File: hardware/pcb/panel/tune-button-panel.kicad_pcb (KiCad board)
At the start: 2 copper layers, 148 x 86.7 mm, 237 parts, among them J1 USB-C, J1 XIAO left, J2 LiPo, J2 XIAO right, J3 Buttons, J3 LiPo, J4 to XIAO BAT, Q1 AO3401A, SW1 MX switch, SW2 MX switch, SW3 MX switch, SW4 MX switch, SW5 RESET, SW6 BOOT, U1 ESP32-C3-WROOM-02-N4, U2 SRV05-4, U3 TP4054, U4 RT9080-3.3, U5 SRV05-4

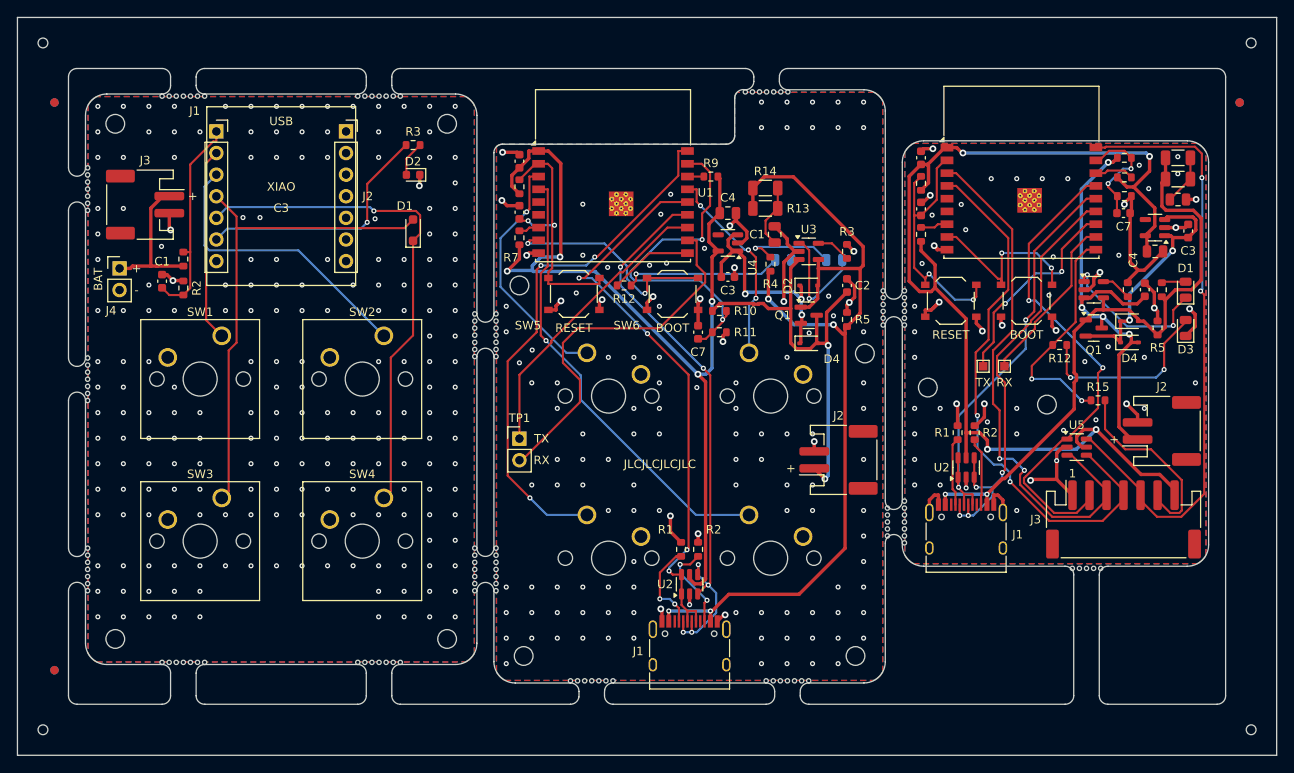
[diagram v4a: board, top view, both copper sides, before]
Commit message: pcb: c3-jst round-8 audit fixes; panel rebuilt with the moved C1
- README: H2 now needs a nylon screw or washers (K2 and VBUS run 1.6 mm from its centre), and the
  c3-jst tab-placement remark follows the new copper.
- Back pour kept off the top edge above the 3V3 track at the antenna base (was a 0.29 mm strip).
- K4 via moved 0.1 mm off K3's (0.60 mm hole to hole).
- panel.py: no tab within 3 mm of an 0805-or-larger ceramic capacitor. Panel rebuilt: c3-jst has six
  tabs, three of them cut-not-snap.
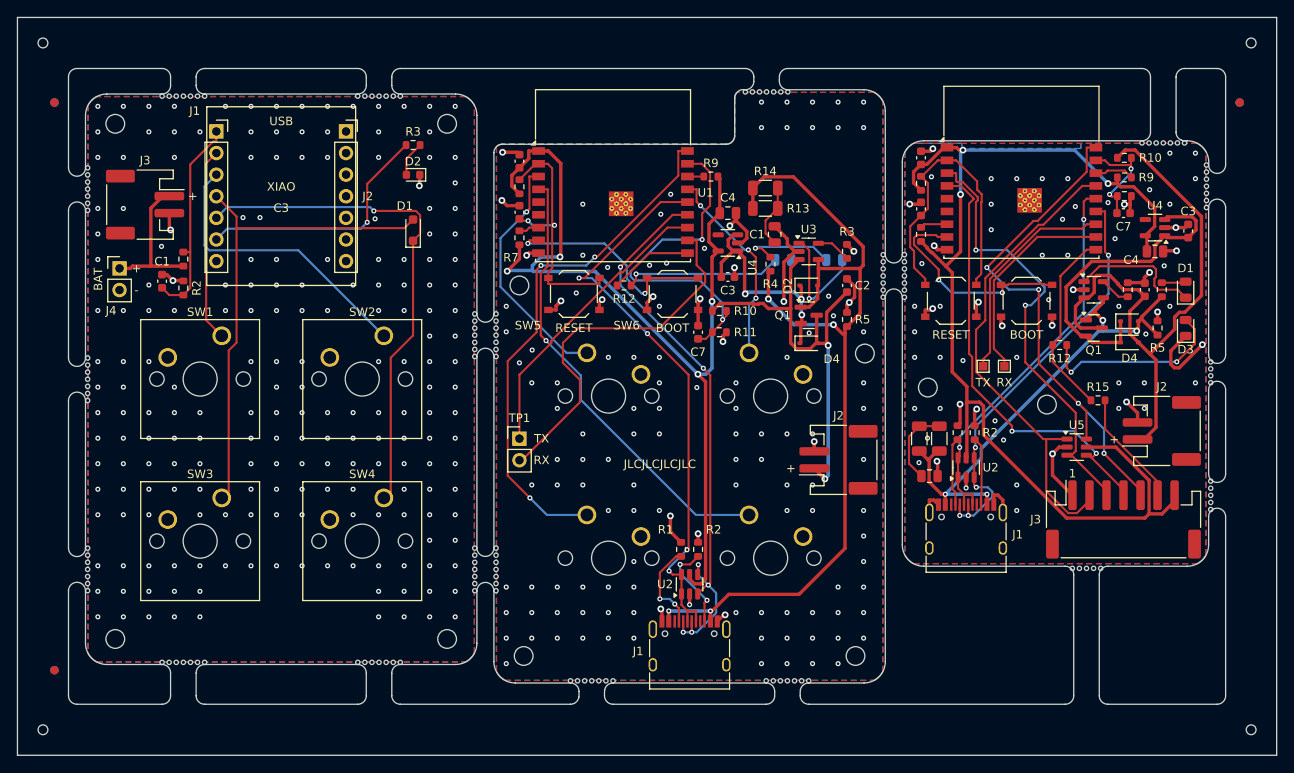
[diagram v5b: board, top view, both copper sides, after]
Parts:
- removed KiKit_MB_19_6: NPTH, NPTH
- added KiKit_MB_12_7: NPTH, NPTH, F.Cu at (101.8, 25.4)
- added KiKit_MB_16_7: NPTH, NPTH, F.Cu at (104.2, 20.4)
- added KiKit_MB_18_1: NPTH, NPTH, F.Cu at (132.2, 7.25)
- added KiKit_MB_18_7: NPTH, NPTH, F.Cu at (137.2, 7.25)
- added KiKit_MB_20_2: NPTH, NPTH, F.Cu at (140.2, 47.0)
- added KiKit_MB_20_3: NPTH, NPTH, F.Cu at (140.2, 47.8)
- added KiKit_MB_20_4: NPTH, NPTH, F.Cu at (140.2, 48.7)
- added KiKit_MB_20_5: NPTH, NPTH, F.Cu at (140.2, 49.5)
- added KiKit_MB_20_6: NPTH, NPTH, F.Cu at (140.2, 50.3)
- added KiKit_MB_21_2: NPTH, NPTH, F.Cu at (127.3, 57.2)
- added KiKit_MB_21_3: NPTH, NPTH, F.Cu at (126.5, 57.2)
- added KiKit_MB_21_4: NPTH, NPTH, F.Cu at (125.7, 57.2)
- added KiKit_MB_21_5: NPTH, NPTH, F.Cu at (124.8, 57.2)
- added KiKit_MB_21_6: NPTH, NPTH, F.Cu at (124.0, 57.2)
- moved KiKit_MB_18_6 57.4 mm to (136.3, 7.25)
- moved KiKit_MB_17_1 56.9 mm to (139.8, 9.84)
- moved KiKit_MB_18_5 56.2 mm to (135.5, 7.25)
- moved KiKit_MB_17_2 55.6 mm to (139.8, 10.7)
- moved KiKit_MB_18_4 55.1 mm to (134.7, 7.25)
- moved KiKit_MB_17_3 54.3 mm to (139.8, 11.5)
- moved KiKit_MB_18_3 53.9 mm to (133.8, 7.25)
- moved KiKit_MB_17_4 53.1 mm to (139.8, 12.3)
- moved KiKit_MB_18_2 52.8 mm to (133.0, 7.25)
- moved KiKit_MB_17_5 51.9 mm to (139.8, 13.2)
- moved KiKit_MB_17_6 50.7 mm to (139.8, 14.0)
- moved KiKit_MB_17_7 49.5 mm to (139.8, 14.8)
- moved R13 44.9 mm to (106.0, 42.0), turned to 90 degrees
- moved C1 43.7 mm to (107.2, 46.4)
- moved R14 41.4 mm to (108.3, 42.0), turned to 90 degrees
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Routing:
- net Board_2-VBAT: track 52.8 -> 69.7 mm, vias 4 -> 0
- net Board_2-GND: track 74.8 -> 58.3 mm, vias 54 -> 64
- net Board_2-K3: track 65.7 -> 51.8 mm
- net Board_2-VBUS: track 73.3 -> 60.9 mm, vias 2 -> 4
- net Board_2-K2: track 64.0 -> 52.2 mm
- net Board_2-K4: track 72.6 -> 61.3 mm, vias 2 -> 4
- net Board_2-VSYS: track 29.0 -> 38.1 mm, vias 2 -> 0
- net Board_2-LED_OUT: track 22.6 -> 13.7 mm
- net Board_2-LED: track 27.0 -> 22.3 mm, vias 2 -> 0
- net Board_2-RXD: track 20.3 -> 24.7 mm
- net Board_2-IO9: track 21.1 -> 25.4 mm
- net Board_2-EN: track 31.4 -> 35.7 mm, vias 2 -> 0
- net Board_2-USB_DP: track 49.3 -> 45.8 mm
- net Board_2-VBUS_C: track 5.89 -> 9.32 mm
- net Board_2-STAT: track 18.3 -> 15.6 mm, vias 2 -> 0
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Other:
- outline, holes or cut-outs redrawn

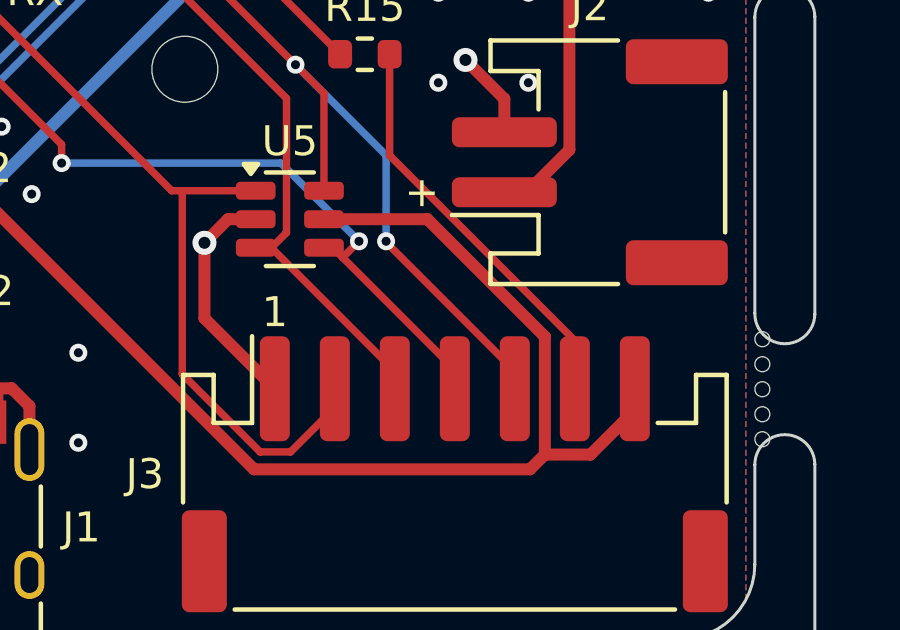
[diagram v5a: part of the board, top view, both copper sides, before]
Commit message: pcb: c3-jst round-9 audit fixes
- README: the single-board right-edge tab windows at 25-29 and 39-45 mm are inside the 2 mm
  connector keep-out, so cut those tabs rather than snapping them; H1's wording names the pour.
- K4: the 0.03 mm stub left by the via move is gone; the diagonal starts at the via, at 45 deg.
- Panel rebuilt with it.
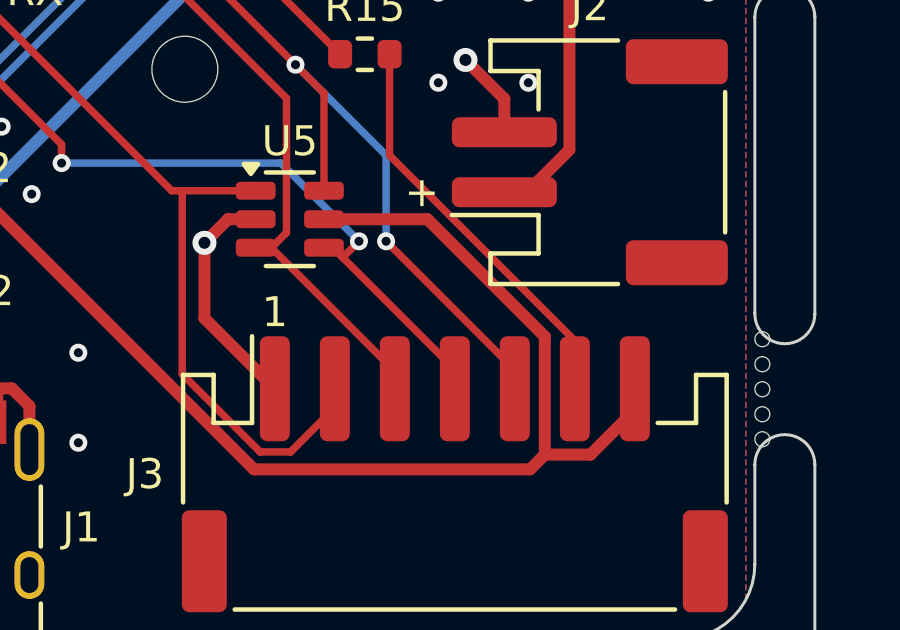
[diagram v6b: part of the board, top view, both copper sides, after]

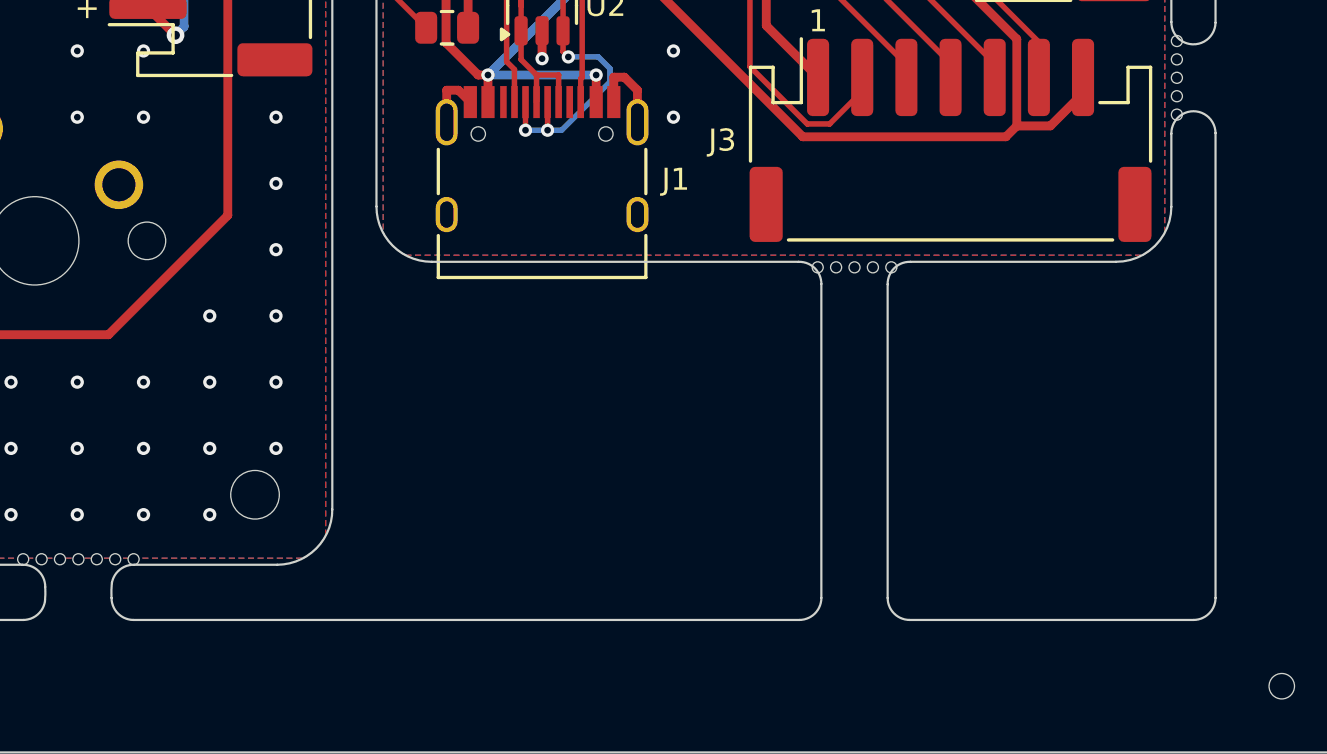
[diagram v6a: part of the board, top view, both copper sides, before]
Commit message: pcb: panel round-7 audit fixes
- Tabs prefer a place at least 2.25 mm from a connector's pads within their free span: c3-jst's
  bottom tab moves clear of J3, leaving two cut-don't-snap tabs (both on c3-jst's right edge).
- Note that pour a tab keepout cuts off is dropped as an island.
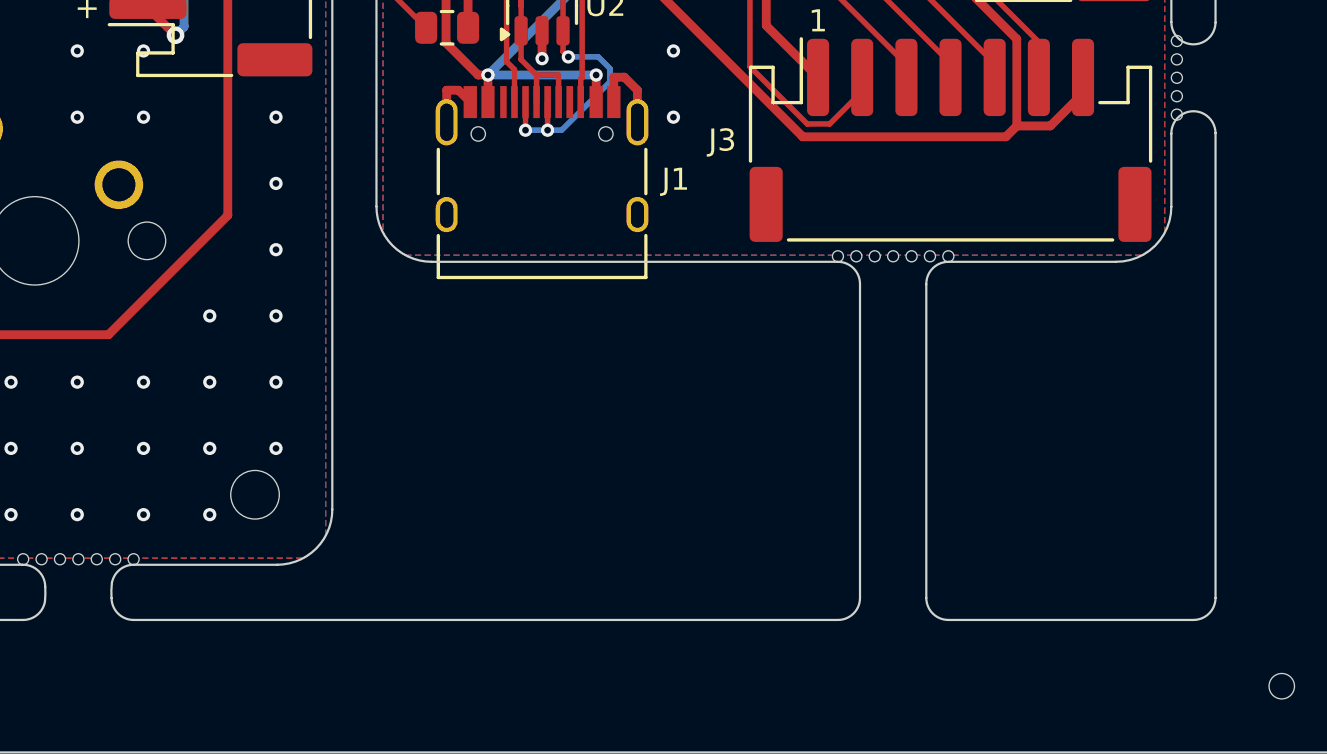
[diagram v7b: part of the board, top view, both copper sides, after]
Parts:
- removed KiKit_MB_20_6: NPTH, NPTH
- added KiKit_MB_19_1: NPTH, NPTH, F.Cu at (129.9, 56.8)
- added KiKit_MB_19_6: NPTH, NPTH, F.Cu at (125.7, 56.8)
- added KiKit_MB_19_7: NPTH, NPTH, F.Cu at (124.9, 56.8)
- moved KiKit_MB_19_2 26.3 mm to (129.1, 56.8)
- moved KiKit_MB_19_3 25.9 mm to (128.2, 56.8)
- moved KiKit_MB_19_4 25.6 mm to (127.4, 56.8)
- moved KiKit_MB_19_5 25.3 mm to (126.6, 56.8)
- moved KiKit_MB_21_6 17.7 mm to (140.2, 50.3)
- moved KiKit_MB_21_5 17.3 mm to (140.2, 49.5)
- moved KiKit_MB_21_4 16.9 mm to (140.2, 48.7)
- moved KiKit_MB_21_3 16.7 mm to (140.2, 47.8)
- moved KiKit_MB_21_2 16.5 mm to (140.2, 47.0)
- moved KiKit_MB_20_5 14.1 mm to (140.2, 35.4)
- moved KiKit_MB_20_4 14.0 mm to (140.2, 34.6)
- moved KiKit_MB_20_3 14.0 mm to (140.2, 33.8)
- moved KiKit_MB_20_2 14.0 mm to (140.2, 33.0)
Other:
- outline, holes or cut-outs redrawn

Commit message: pcb: c3-jst: RC damper (R16 1 ohm + C8 10 uF) at the RT9080 input, rerouted
sim12 had VSYS ringing to 6.6-6.7 V on a no-cell hot-plug against the RT9080's 6.5 V; sim13 puts
the damped worst case at 5.86 V. Panel rebuilt; README tab gaps and cutoff figures updated.
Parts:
- added C8: 10u, Capacitor_SMD:C_0805_2012Metric, F.Cu at (136.4, 11.5)
- added KiKit_MB_20_1: NPTH, NPTH, F.Cu at (130.9, 56.8)
- added KiKit_MB_20_6: NPTH, NPTH, F.Cu at (126.8, 56.8)
- added KiKit_MB_20_7: NPTH, NPTH, F.Cu at (125.9, 56.8)
- added KiKit_MB_22_2: NPTH, NPTH, F.Cu at (140.2, 47.0)
- added KiKit_MB_22_3: NPTH, NPTH, F.Cu at (140.2, 47.8)
- added KiKit_MB_22_4: NPTH, NPTH, F.Cu at (140.2, 48.7)
- added KiKit_MB_22_5: NPTH, NPTH, F.Cu at (140.2, 49.5)
- added KiKit_MB_22_6: NPTH, NPTH, F.Cu at (140.2, 50.3)
- added R16: 1, Resistor_SMD:R_1206_3216Metric, F.Cu at (136.4, 13.9)
- moved KiKit_MB_14_7 73.8 mm to (90.6, 1.25)
- moved KiKit_MB_14_6 73.2 mm to (89.7, 1.25)
- moved KiKit_MB_14_5 72.7 mm to (88.9, 1.25)
- moved KiKit_MB_14_4 72.2 mm to (88.0, 1.25)
- moved KiKit_MB_14_3 71.7 mm to (87.2, 1.25)
- moved KiKit_MB_14_2 71.3 mm to (86.4, 1.25)
- moved KiKit_MB_14_1 70.9 mm to (85.5, 1.25)
- moved KiKit_MB_16_7 52.7 mm to (88.0, 70.5)
- moved KiKit_MB_16_6 51.6 mm to (88.8, 70.5)
- moved KiKit_MB_16_5 50.6 mm to (89.7, 70.5)
- moved KiKit_MB_19_7 50.2 mm to (133.3, 7.25)
- moved KiKit_MB_19_6 50.0 mm to (132.5, 7.25)
- moved KiKit_MB_19_5 49.8 mm to (131.6, 7.25)
- moved KiKit_MB_19_4 49.6 mm to (130.8, 7.25)
- moved KiKit_MB_16_4 49.5 mm to (90.5, 70.5)
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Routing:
- net Board_2-VBAT: track 69.7 -> 51.3 mm
- net Board_2-K4: track 61.2 -> 74.6 mm, vias 4 -> 3
- net Board_2-IO2: track 4.63 -> 15.2 mm, vias 0 -> 2
- net Board_2-LED_OUT: track 13.7 -> 22.0 mm, vias 0 -> 2
- net Board_2-USB_DP: track 45.8 -> 53.0 mm
- net Board_2-K2: track 52.2 -> 59.3 mm
- net Board_2-LED_A: track 22.6 -> 15.7 mm
- net Board_2-VBAT_SENSE: track 12.7 -> 19.6 mm
- net Board_2-VSYS: track 38.1 -> 32.5 mm, vias 0 -> 2
- net Board_2-USB_DN: track 50.3 -> 55.0 mm, vias 5 -> 4
- net Board_2-K1: track 56.4 -> 51.8 mm, vias 0 -> 4
- net Board_2-3V3: track 130.1 -> 134.6 mm, vias 3 -> 2
- net Board_2-RXD: track 24.7 -> 20.3 mm
- net Board_2-PROG: track 3.60 -> 7.66 mm, vias 0 -> 2
- net Board_2-GND: track 58.3 -> 62.1 mm, vias 64 -> 66
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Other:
- outline, holes or cut-outs redrawn
